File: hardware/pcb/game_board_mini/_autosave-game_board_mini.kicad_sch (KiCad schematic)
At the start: 8 parts, among them J1 Conn_01x08, J3 Conn_01x03, J4 Conn_01x03, J5 Conn_01x03

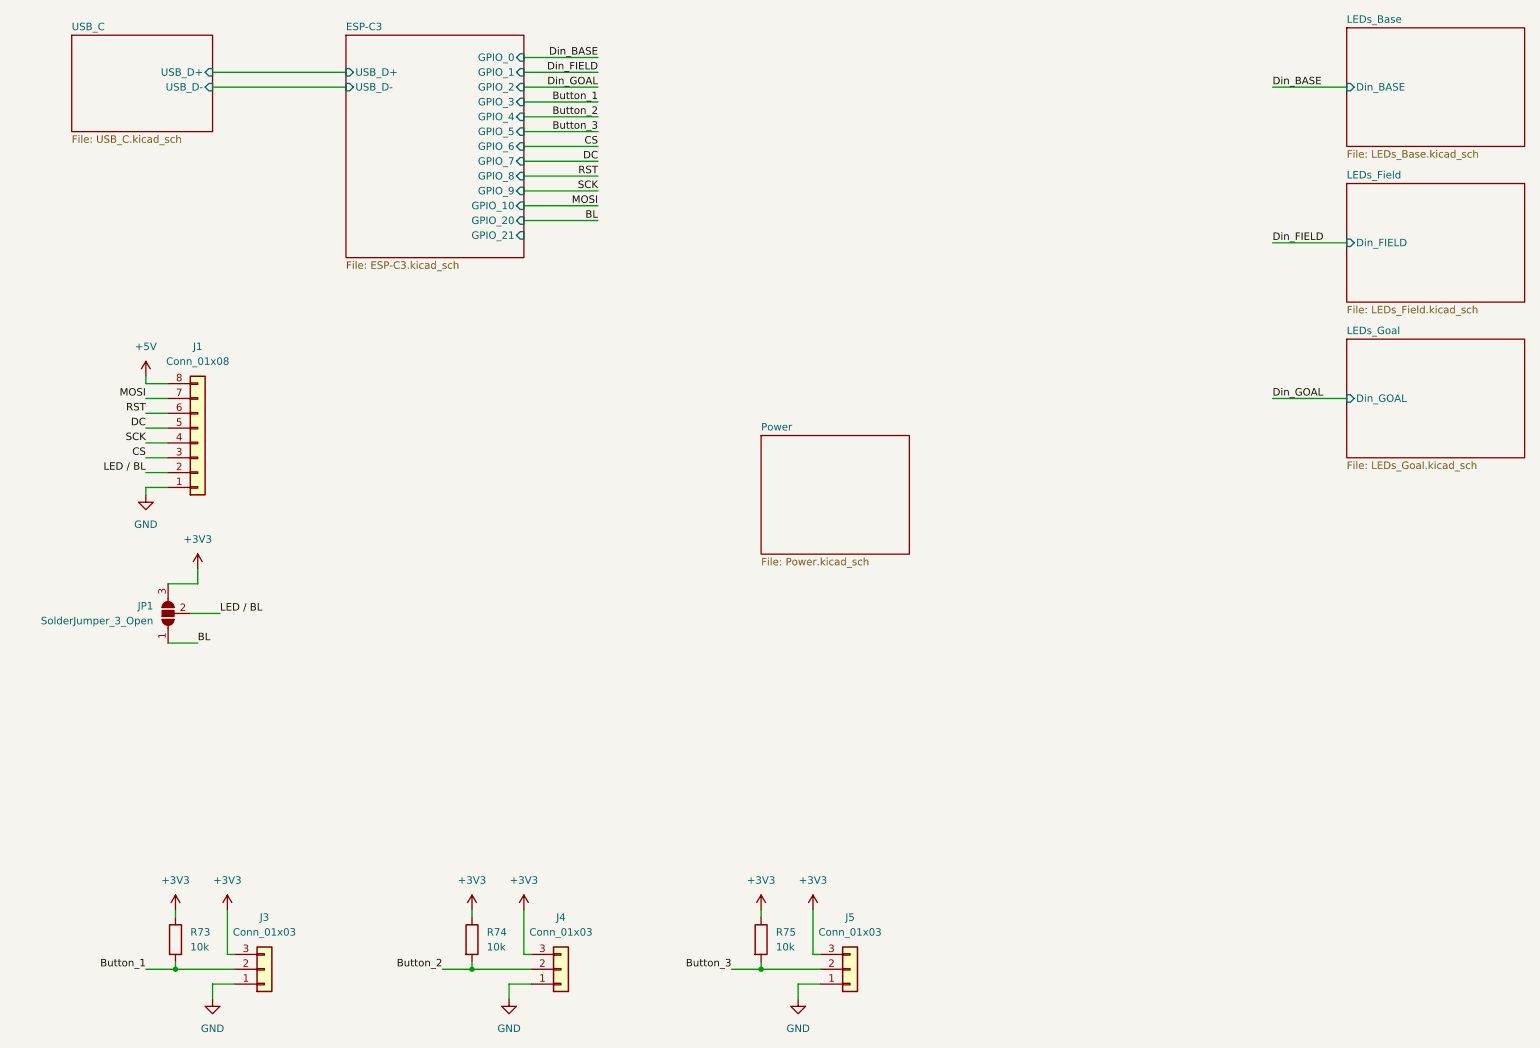
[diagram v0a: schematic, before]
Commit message: Fixed bug: `player_count` and `brightness` reset in loop
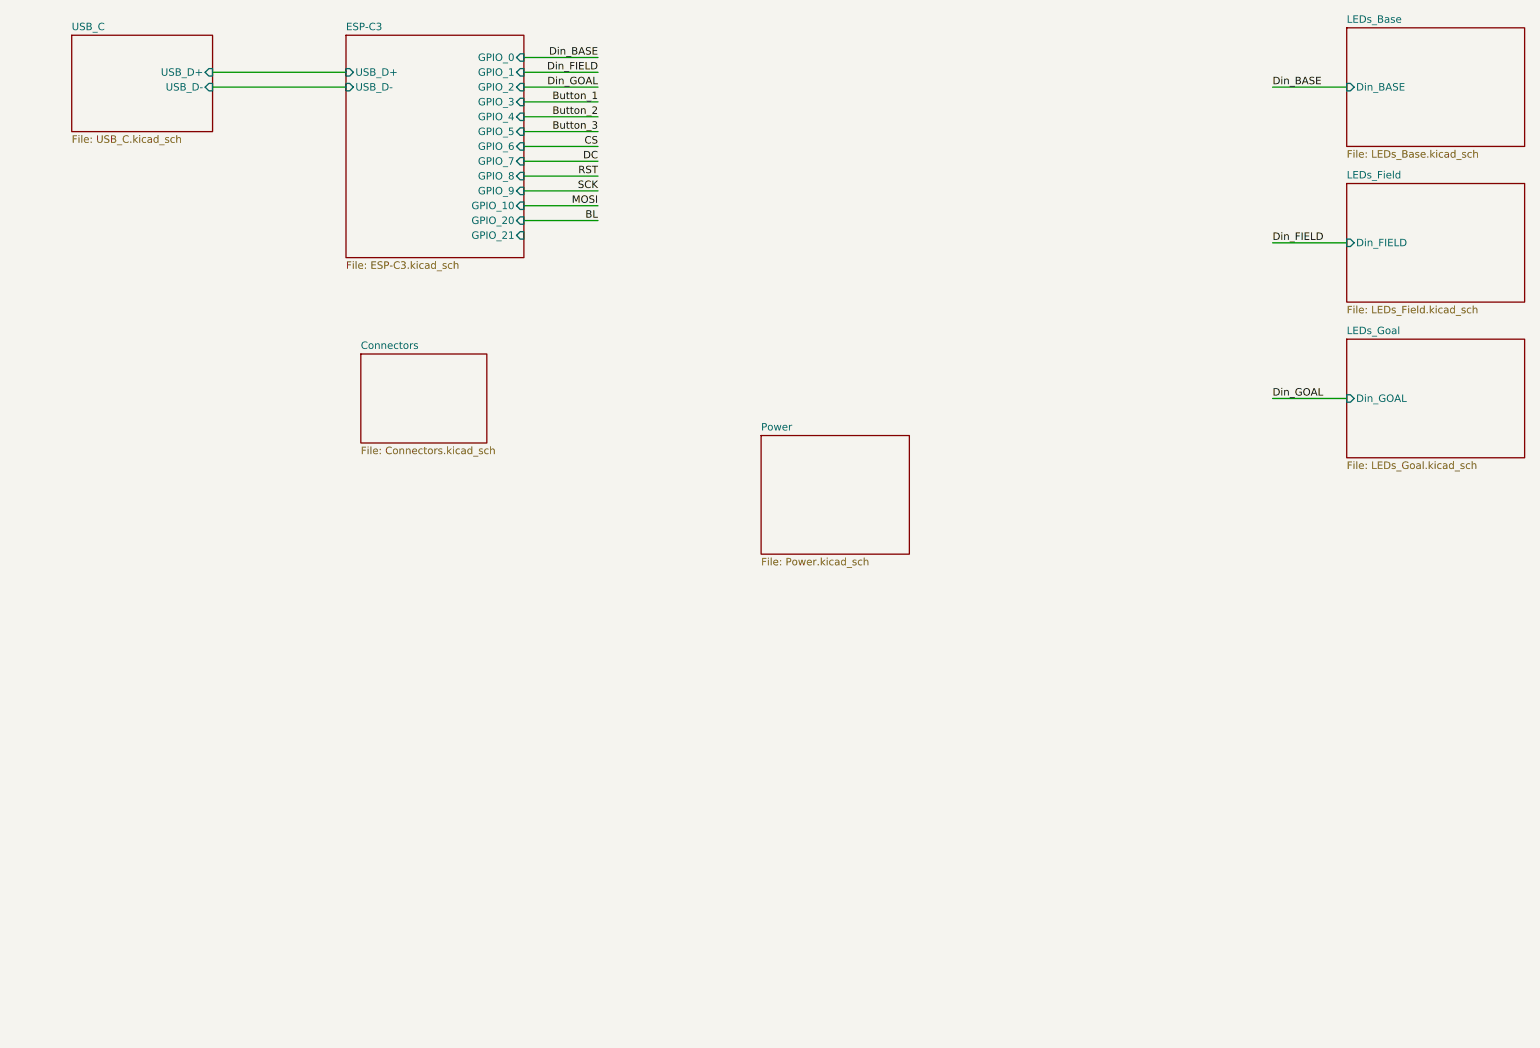
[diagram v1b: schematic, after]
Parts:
- removed J1: Conn_01x08, Connector_JST:JST_PH_B8B-PH-K_1x08_P2.00mm_Vertical, symbol Connector_Generic:Conn_01x08
- removed J3, J4, J5: Conn_01x03, Connector_JST:JST_PH_B3B-PH-K_1x03_P2.00mm_Vertical, symbol Connector_Generic:Conn_01x03
- removed JP1: SolderJumper_3_Open, Jumper:SolderJumper-3_P1.3mm_Open_Pad1.0x1.5mm, symbol Jumper:SolderJumper_3_Open
- removed R73, R74, R75: 10k, Resistor_SMD:R_0805_2012Metric, symbol Device:R
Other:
- added sheet Connectors (Connectors.kicad_sch)
